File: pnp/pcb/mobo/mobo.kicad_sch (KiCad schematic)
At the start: 0 parts

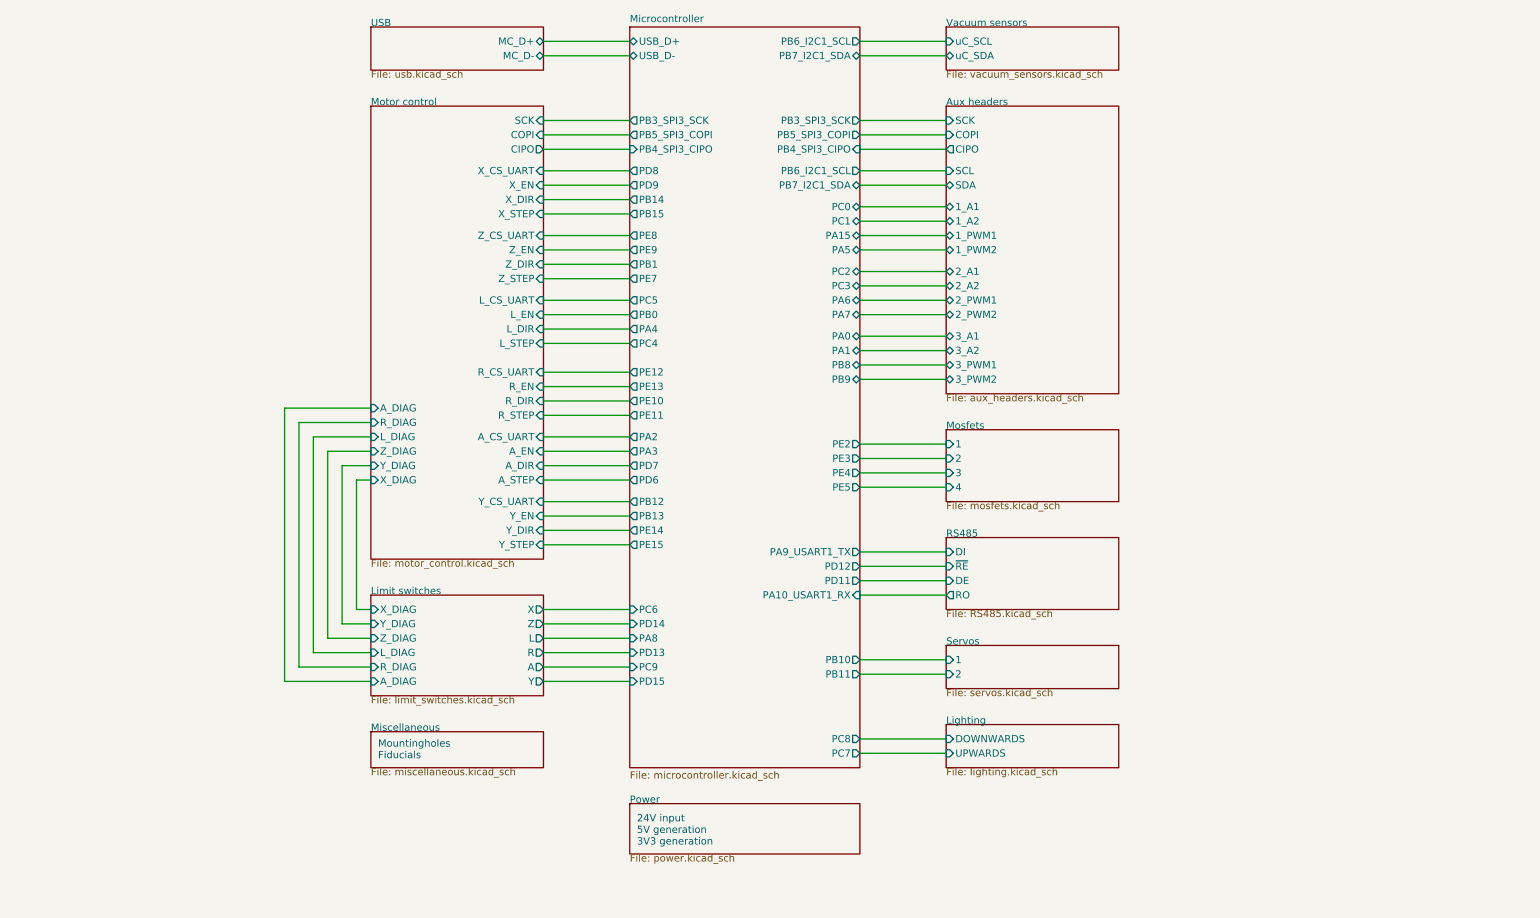
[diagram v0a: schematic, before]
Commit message: Mobo V4A Redesign
Some EMC improvements to schematics.
Reassigned MCU Pins for HW-PWM support.
Changes are still marked with text in the schematics.
Complete PCB Layout reworked
Status: Needs to be verified, and cleaned up a little, but DRC is running green.
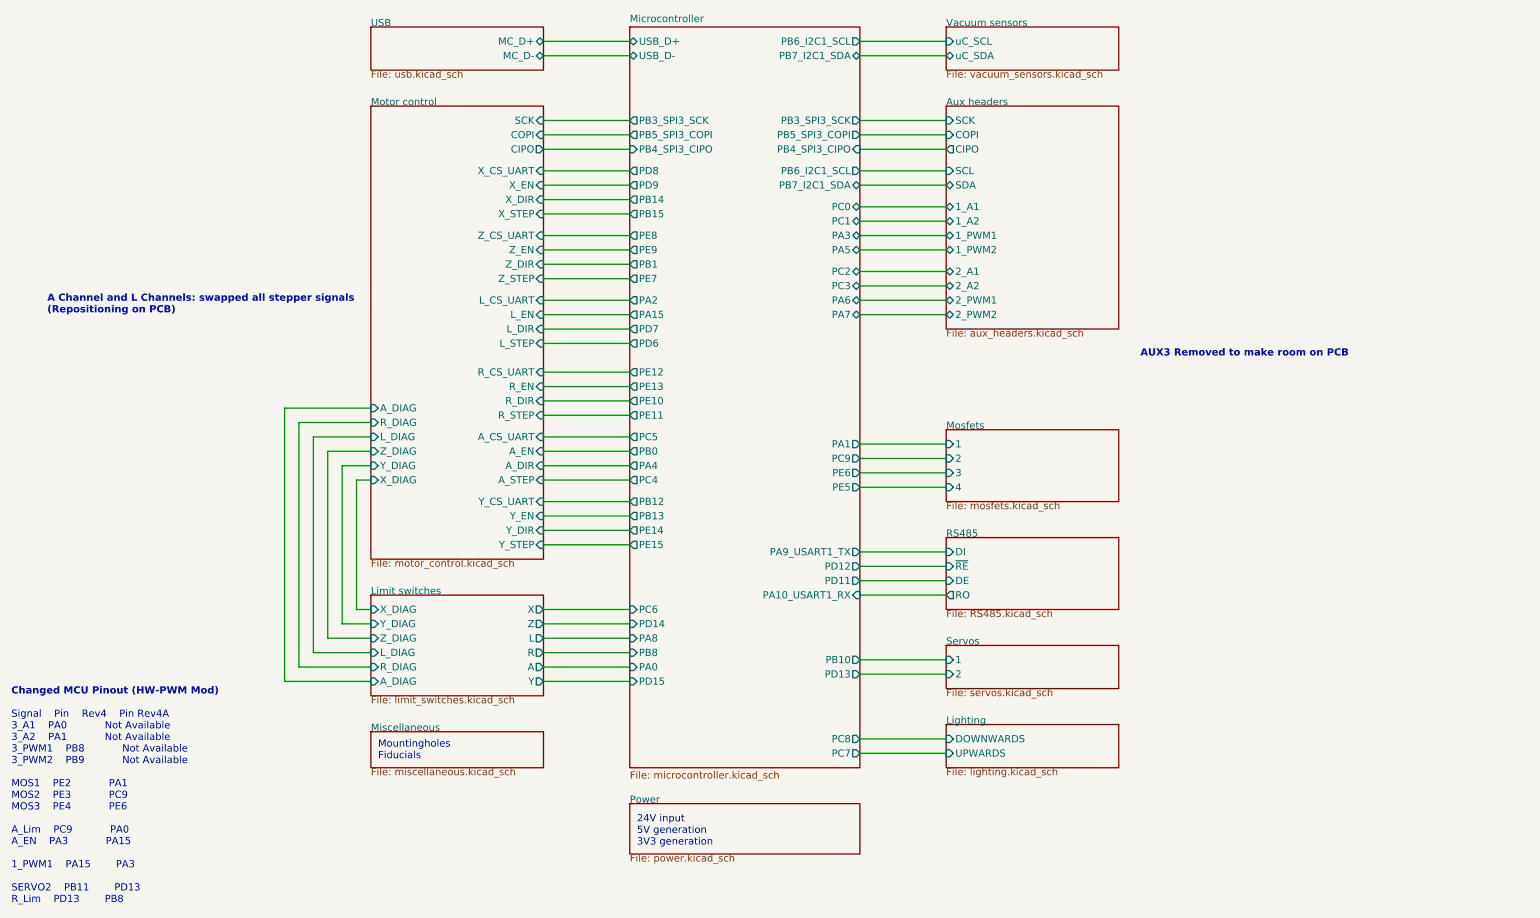
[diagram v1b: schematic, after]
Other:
- sheet Aux headers ports: added none; removed 3_A1, 3_A2, 3_PWM1, 3_PWM2
- sheet Microcontroller ports: added PE6; removed PB11, PB9, PE2, PE3, PE4
- note added: "A Channel and L Channels: swapped all stepper signals (Repositioning on PCB)"
- note added: "AUX3 Removed to make room on PCB"
- note added: "Changed MCU Pinout (HW-PWM Mod)"
- note added: "Signal Pin Rev4 Pin Rev4A 3_A1 PA0 Not Available 3_A2 PA1 Not Available 3_PWM1 PB8 Not Available 3_PWM2 PB9 Not Available MOS1 PE2 PA1 MOS2 PE3 PC9 MOS3 PE4 PE6 A_Lim PC9 PA0 A_EN PA3 PA15 1_PWM1 PA15 PA3 SERVO2 PB11 PD13 R_Lim PD13 PB8"

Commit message: Redesign finished
Completed Board redesign and adding more EMC improvements.
Changed all the part numbers to have a Mouser orderable design (except the JST connectors)
All outputs generated
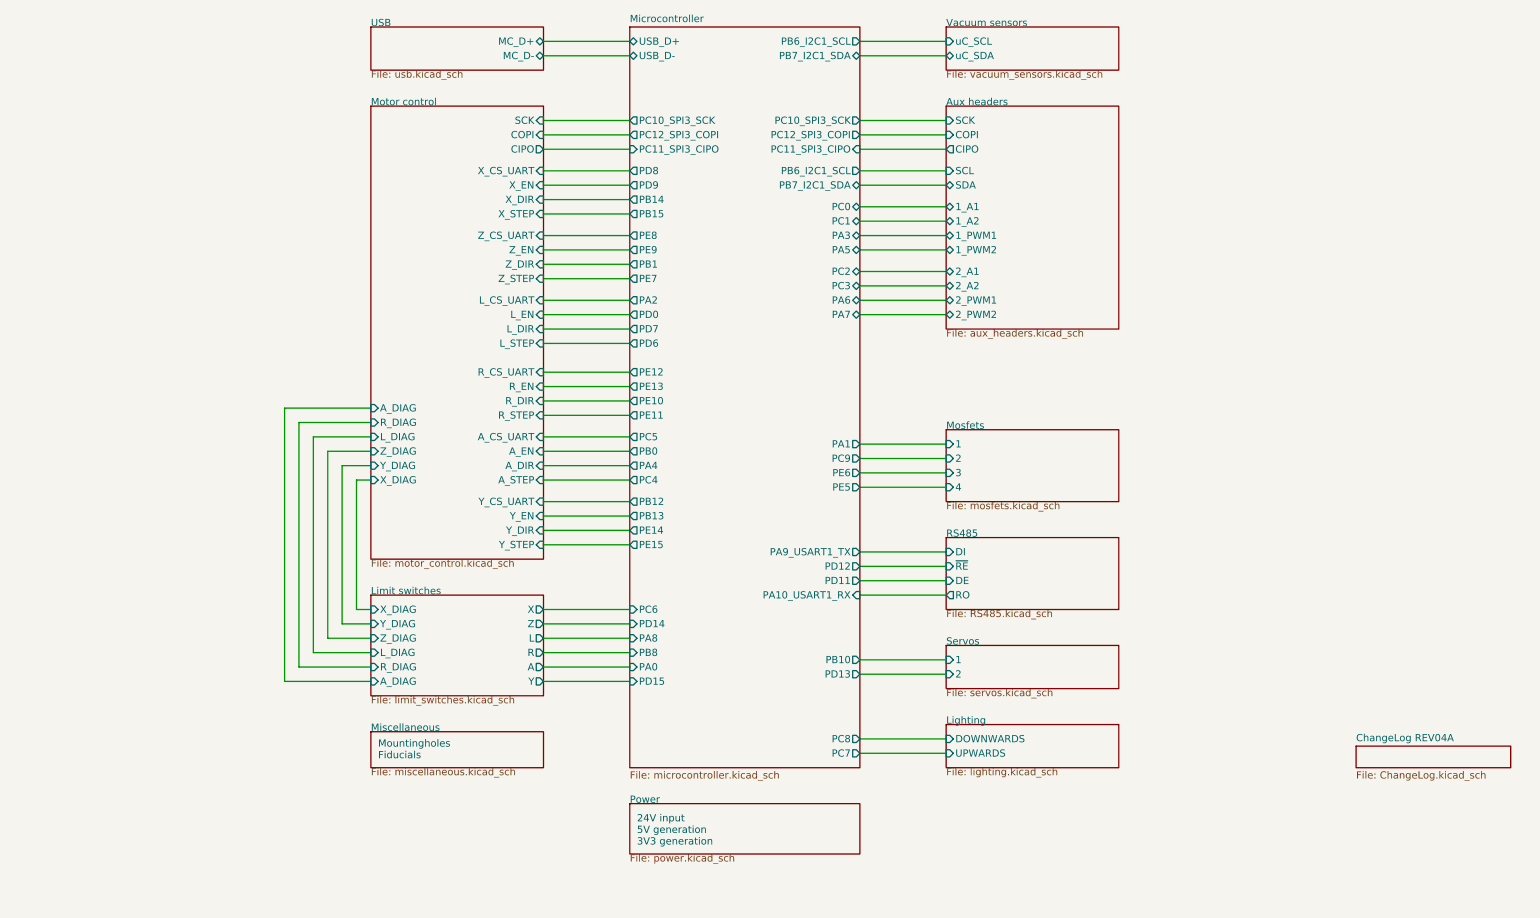
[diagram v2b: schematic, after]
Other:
- added sheet ChangeLog REV04A (ChangeLog.kicad_sch)
- sheet Microcontroller ports: added PC10_SPI3_SCK, PC11_SPI3_CIPO, PC12_SPI3_COPI, PD0; removed PA15, PB3_SPI3_SCK, PB4_SPI3_CIPO, PB5_SPI3_COPI
- note removed: "A Channel and L Channels: swapped all stepper signals (Repositioning on PCB)"
- note removed: "AUX3 Removed to make room on PCB"
- note removed: "Changed MCU Pinout (HW-PWM Mod)"
- note removed: "Signal Pin Rev4 Pin Rev4A 3_A1 PA0 Not Available 3_A2 PA1 Not Available 3_PWM1 PB8 Not Available 3_PWM2 PB9 Not Available MOS1 PE2 PA1 MOS2 PE3 PC9 MOS3 PE4 PE6 A_Lim PC9 PA0 A_EN PA3 PA15 1_PWM1 PA15 PA3 SERVO2 PB11 PD13 R_Lim PD13 PB8"
- company: Opulo -> Opulo.io
